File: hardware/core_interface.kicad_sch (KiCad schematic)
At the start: 2 parts, among them J90 Core_LGA, J91 Core_LGA

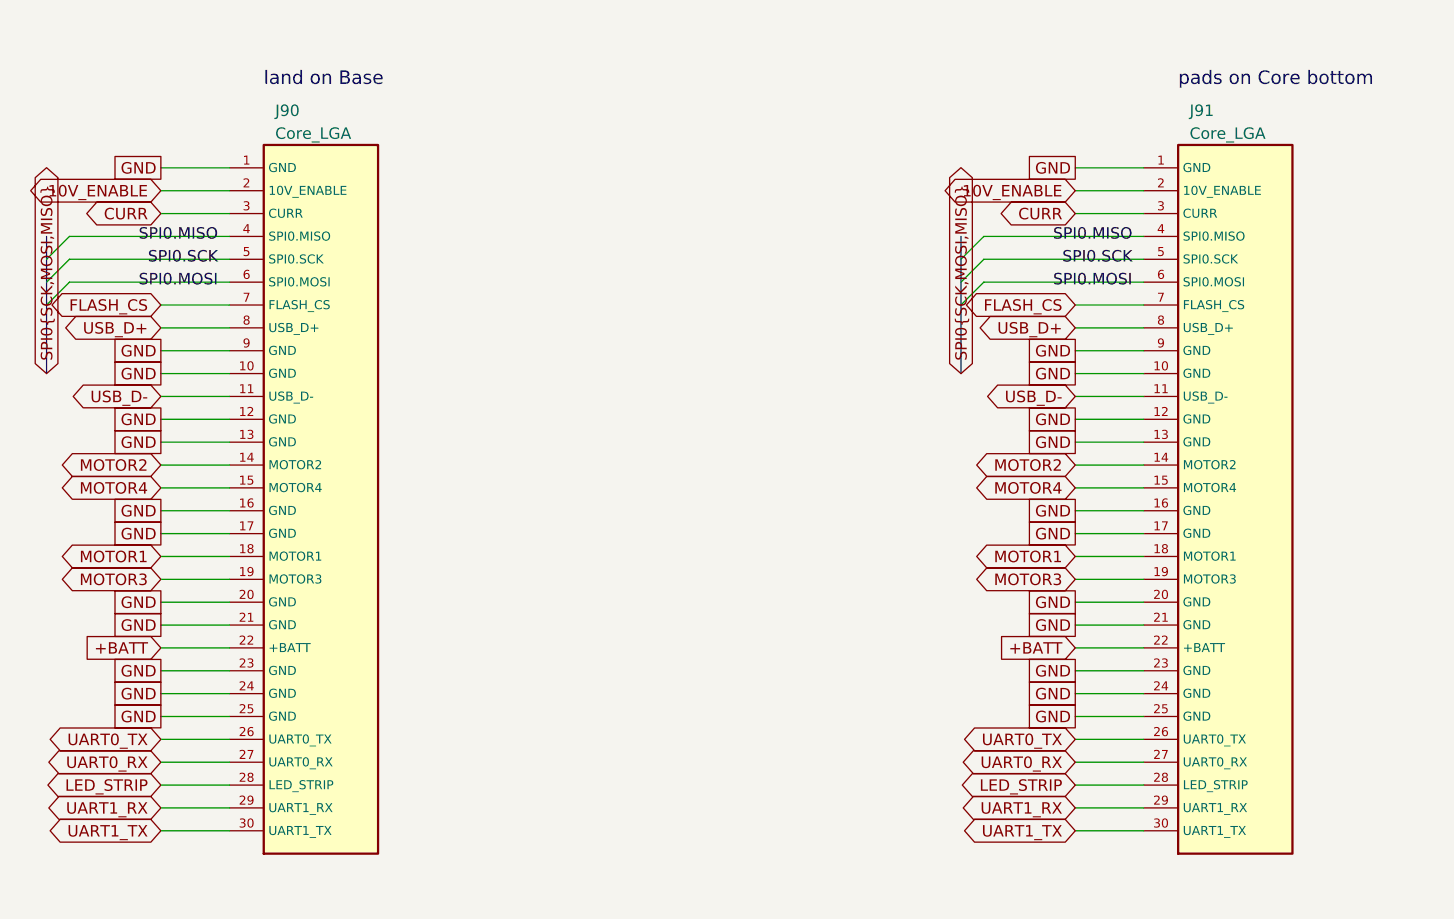
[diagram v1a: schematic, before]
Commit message: OpenAIO: LGA 31 pins (+5V and BUZZER- added, stray GND removed), J91 follows the pattern centre automatically
Co-Authored-By: Claude Fable 5 <noreply@anthropic.com>
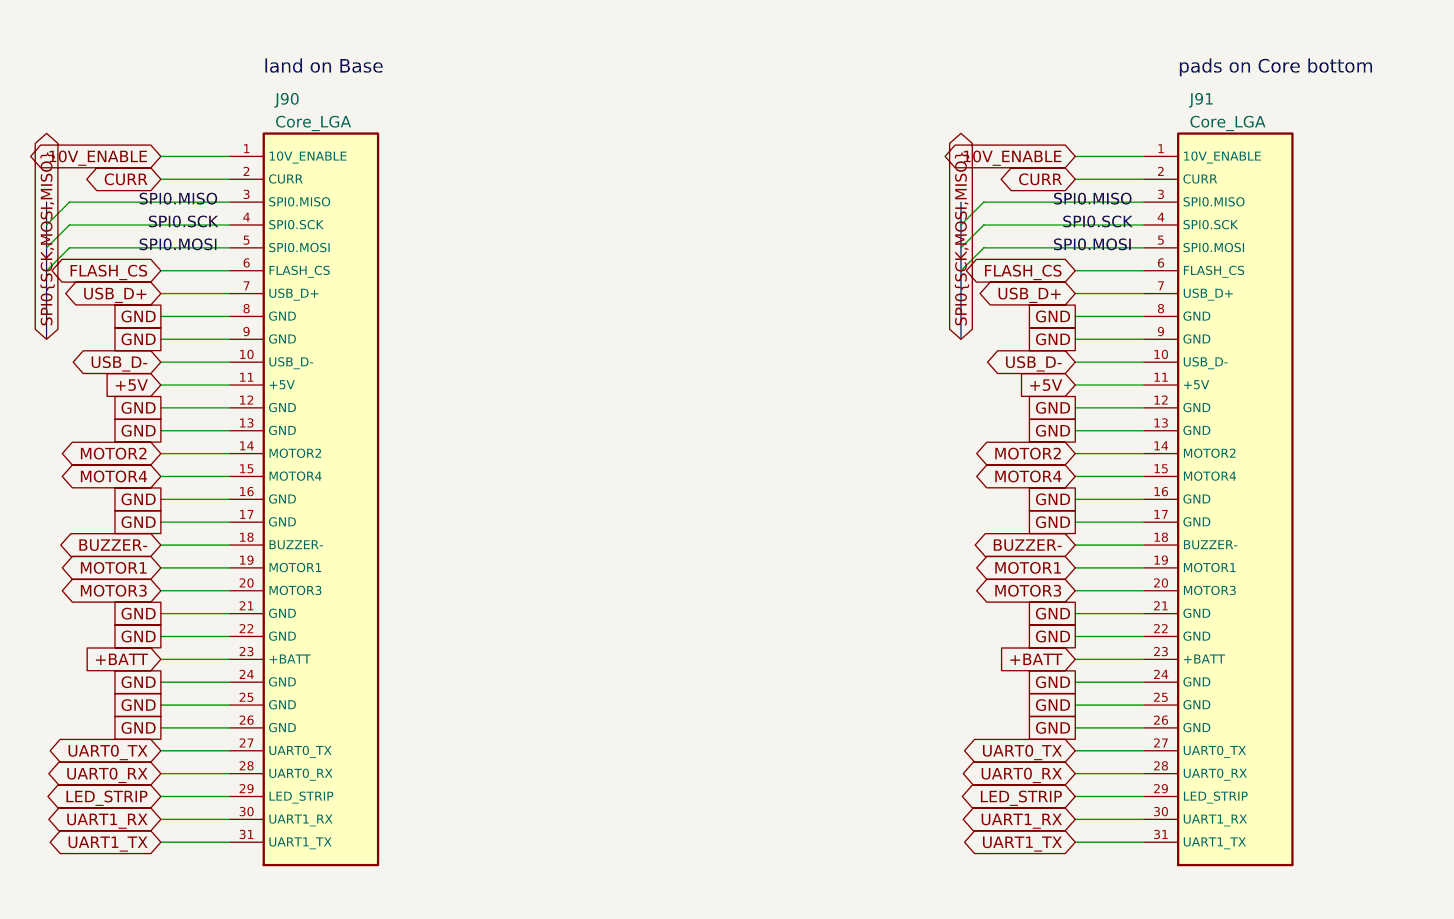
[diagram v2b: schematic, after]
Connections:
- net +BATT: now also J90.23 (+BATT), J91.23 (+BATT); no longer J90.22 (+BATT), J91.22 (+BATT)
- net 10V_ENABLE: now also J90.1 (10V_ENABLE), J91.1 (10V_ENABLE); no longer J90.2 (10V_ENABLE), J91.2 (10V_ENABLE)
- net CURR: now also J90.2 (CURR), J91.2 (CURR); no longer J90.3 (CURR), J91.3 (CURR)
- net FLASH_CS: now also J90.6 (FLASH_CS), J91.6 (FLASH_CS); no longer J90.7 (FLASH_CS), J91.7 (FLASH_CS)
- net GND: now also J90.22 (GND), J90.26 (GND), J90.8 (GND), J91.22 (GND), J91.26 (GND), J91.8 (GND); no longer J90.1 (GND), J90.10 (GND), J90.20 (GND), J90.23 (GND), J91.1 (GND), J91.10 (GND), J91.20 (GND), J91.23 (GND)
- net LED_STRIP: now also J90.29 (LED_STRIP), J91.29 (LED_STRIP); no longer J90.28 (LED_STRIP), J91.28 (LED_STRIP)
- net MOTOR1: now also J90.19 (MOTOR1), J91.19 (MOTOR1); no longer J90.18 (MOTOR1), J91.18 (MOTOR1)
- net MOTOR3: now also J90.20 (MOTOR3), J91.20 (MOTOR3); no longer J90.19 (MOTOR3), J91.19 (MOTOR3)
- net SPI0.MISO: now also J90.3 (SPI0.MISO), J91.3 (SPI0.MISO); no longer J90.4 (SPI0.MISO), J91.4 (SPI0.MISO)
- net SPI0.MOSI: now also J90.5 (SPI0.MOSI), J91.5 (SPI0.MOSI); no longer J90.6 (SPI0.MOSI), J91.6 (SPI0.MOSI)
- net SPI0.SCK: now also J90.4 (SPI0.SCK), J91.4 (SPI0.SCK); no longer J90.5 (SPI0.SCK), J91.5 (SPI0.SCK)
- net UART0_RX: now also J90.28 (UART0_RX), J91.28 (UART0_RX); no longer J90.27 (UART0_RX), J91.27 (UART0_RX)
- net UART0_TX: now also J90.27 (UART0_TX), J91.27 (UART0_TX); no longer J90.26 (UART0_TX), J91.26 (UART0_TX)
- net UART1_RX: now also J90.30 (UART1_RX), J91.30 (UART1_RX); no longer J90.29 (UART1_RX), J91.29 (UART1_RX)
- net UART1_TX: now also J90.31 (UART1_TX), J91.31 (UART1_TX); no longer J90.30 (UART1_TX), J91.30 (UART1_TX)
- net USB_D+: now also J90.7 (USB_D+), J91.7 (USB_D+); no longer J90.8 (USB_D+), J91.8 (USB_D+)
- net USB_D-: now also J90.10 (USB_D-), J91.10 (USB_D-); no longer J90.11 (USB_D-), J91.11 (USB_D-)
- new net +5V: J90.11 (+5V), J91.11 (+5V)
- new net BUZZER-: J90.18 (BUZZER-), J91.18 (BUZZER-)

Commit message: OpenAIO: LGA +10V pin added
Co-Authored-By: Claude Fable 5 <noreply@anthropic.com>
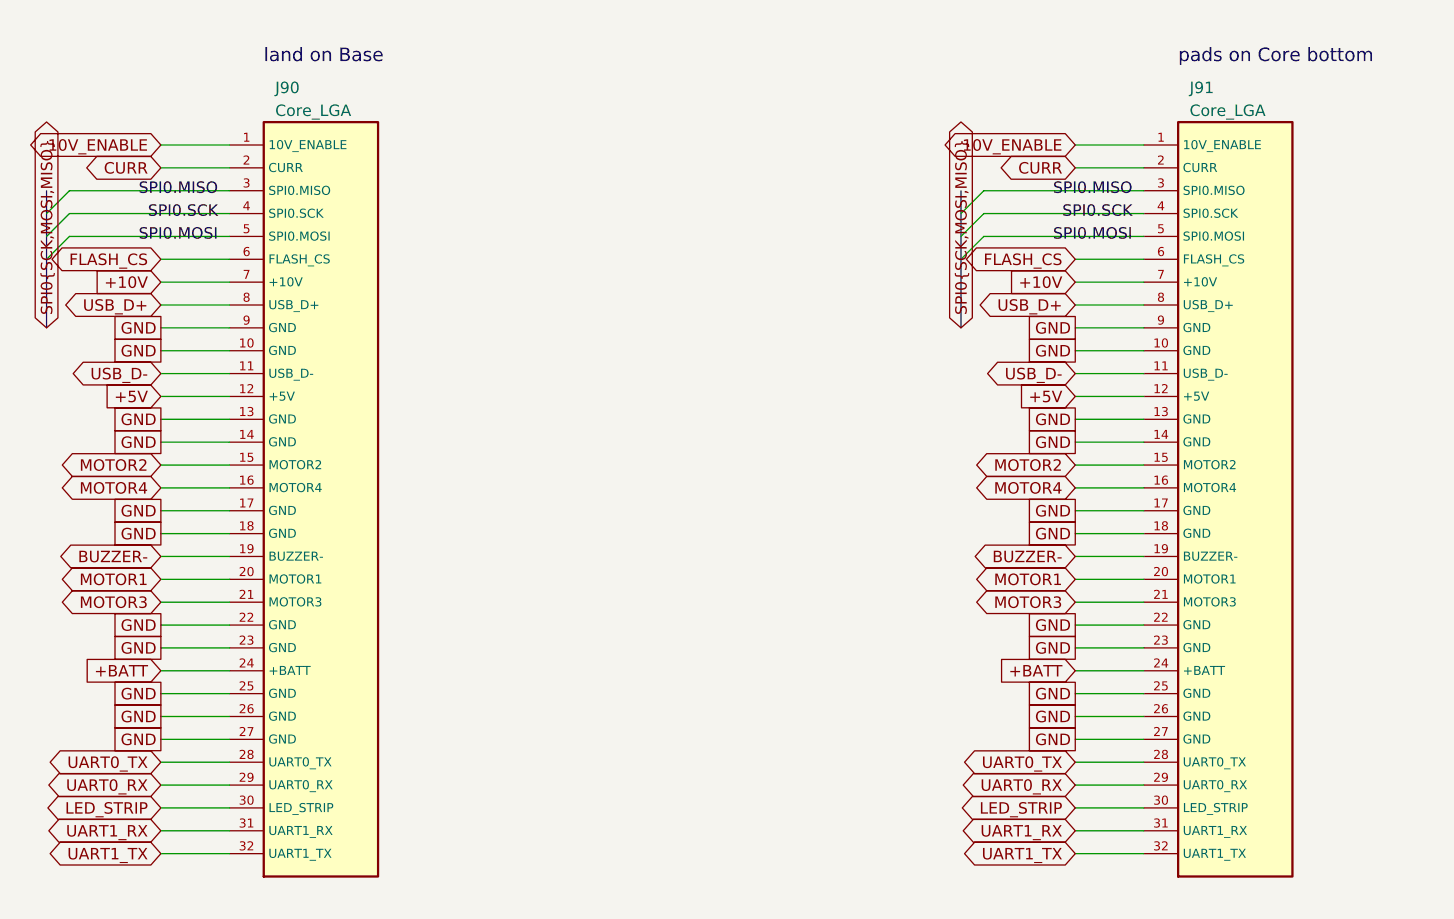
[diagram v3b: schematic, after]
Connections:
- net +5V: now also J90.12 (+5V), J91.12 (+5V); no longer J90.11 (+5V), J91.11 (+5V)
- net +BATT: now also J90.24 (+BATT), J91.24 (+BATT); no longer J90.23 (+BATT), J91.23 (+BATT)
- net BUZZER-: now also J90.19 (BUZZER-), J91.19 (BUZZER-); no longer J90.18 (BUZZER-), J91.18 (BUZZER-)
- net GND: now also J90.10 (GND), J90.14 (GND), J90.18 (GND), J90.23 (GND), J90.27 (GND), J91.10 (GND), J91.14 (GND), J91.18 (GND), J91.23 (GND), J91.27 (GND); no longer J90.12 (GND), J90.16 (GND), J90.21 (GND), J90.24 (GND), J90.8 (GND), J91.12 (GND), J91.16 (GND), J91.21 (GND), J91.24 (GND), J91.8 (GND)
- net LED_STRIP: now also J90.30 (LED_STRIP), J91.30 (LED_STRIP); no longer J90.29 (LED_STRIP), J91.29 (LED_STRIP)
- net MOTOR1: now also J90.20 (MOTOR1), J91.20 (MOTOR1); no longer J90.19 (MOTOR1), J91.19 (MOTOR1)
- net MOTOR2: now also J90.15 (MOTOR2), J91.15 (MOTOR2); no longer J90.14 (MOTOR2), J91.14 (MOTOR2)
- net MOTOR3: now also J90.21 (MOTOR3), J91.21 (MOTOR3); no longer J90.20 (MOTOR3), J91.20 (MOTOR3)
- net MOTOR4: now also J90.16 (MOTOR4), J91.16 (MOTOR4); no longer J90.15 (MOTOR4), J91.15 (MOTOR4)
- net UART0_RX: now also J90.29 (UART0_RX), J91.29 (UART0_RX); no longer J90.28 (UART0_RX), J91.28 (UART0_RX)
- net UART0_TX: now also J90.28 (UART0_TX), J91.28 (UART0_TX); no longer J90.27 (UART0_TX), J91.27 (UART0_TX)
- net UART1_RX: now also J90.31 (UART1_RX), J91.31 (UART1_RX); no longer J90.30 (UART1_RX), J91.30 (UART1_RX)
- net UART1_TX: now also J90.32 (UART1_TX), J91.32 (UART1_TX); no longer J90.31 (UART1_TX), J91.31 (UART1_TX)
- net USB_D+: now also J90.8 (USB_D+), J91.8 (USB_D+); no longer J90.7 (USB_D+), J91.7 (USB_D+)
- net USB_D-: now also J90.11 (USB_D-), J91.11 (USB_D-); no longer J90.10 (USB_D-), J91.10 (USB_D-)
- new net +10V: J90.7 (+10V), J91.7 (+10V)

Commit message: OpenAIO: LGA +3.3V pin added
Co-Authored-By: Claude Fable 5 <noreply@anthropic.com>
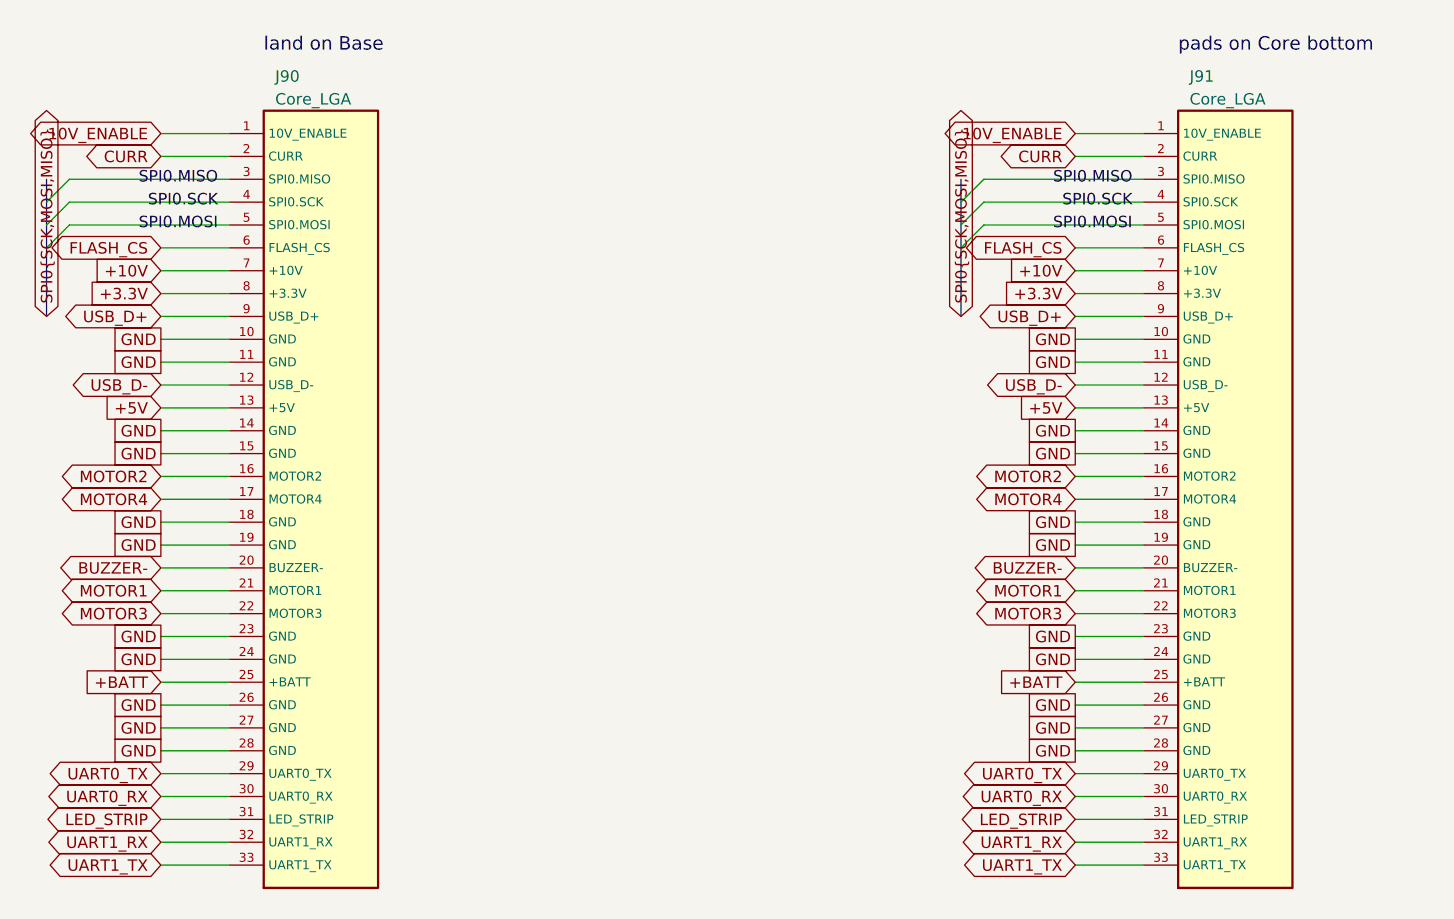
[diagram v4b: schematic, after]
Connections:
- net +5V: now also J90.13 (+5V), J91.13 (+5V); no longer J90.12 (+5V), J91.12 (+5V)
- net +BATT: now also J90.25 (+BATT), J91.25 (+BATT); no longer J90.24 (+BATT), J91.24 (+BATT)
- net BUZZER-: now also J90.20 (BUZZER-), J91.20 (BUZZER-); no longer J90.19 (BUZZER-), J91.19 (BUZZER-)
- net GND: now also J90.11 (GND), J90.15 (GND), J90.19 (GND), J90.24 (GND), J90.28 (GND), J91.11 (GND), J91.15 (GND), J91.19 (GND), J91.24 (GND), J91.28 (GND); no longer J90.13 (GND), J90.17 (GND), J90.22 (GND), J90.25 (GND), J90.9 (GND), J91.13 (GND), J91.17 (GND), J91.22 (GND), J91.25 (GND), J91.9 (GND)
- net LED_STRIP: now also J90.31 (LED_STRIP), J91.31 (LED_STRIP); no longer J90.30 (LED_STRIP), J91.30 (LED_STRIP)
- net MOTOR1: now also J90.21 (MOTOR1), J91.21 (MOTOR1); no longer J90.20 (MOTOR1), J91.20 (MOTOR1)
- net MOTOR2: now also J90.16 (MOTOR2), J91.16 (MOTOR2); no longer J90.15 (MOTOR2), J91.15 (MOTOR2)
- net MOTOR3: now also J90.22 (MOTOR3), J91.22 (MOTOR3); no longer J90.21 (MOTOR3), J91.21 (MOTOR3)
- net MOTOR4: now also J90.17 (MOTOR4), J91.17 (MOTOR4); no longer J90.16 (MOTOR4), J91.16 (MOTOR4)
- net UART0_RX: now also J90.30 (UART0_RX), J91.30 (UART0_RX); no longer J90.29 (UART0_RX), J91.29 (UART0_RX)
- net UART0_TX: now also J90.29 (UART0_TX), J91.29 (UART0_TX); no longer J90.28 (UART0_TX), J91.28 (UART0_TX)
- net UART1_RX: now also J90.32 (UART1_RX), J91.32 (UART1_RX); no longer J90.31 (UART1_RX), J91.31 (UART1_RX)
- net UART1_TX: now also J90.33 (UART1_TX), J91.33 (UART1_TX); no longer J90.32 (UART1_TX), J91.32 (UART1_TX)
- net USB_D+: now also J90.9 (USB_D+), J91.9 (USB_D+); no longer J90.8 (USB_D+), J91.8 (USB_D+)
- net USB_D-: now also J90.12 (USB_D-), J91.12 (USB_D-); no longer J90.11 (USB_D-), J91.11 (USB_D-)
- new net +3.3V: J90.8 (+3.3V), J91.8 (+3.3V)

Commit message: OpenAIO: LGA +4v5 pin added
Co-Authored-By: Claude Fable 5 <noreply@anthropic.com>
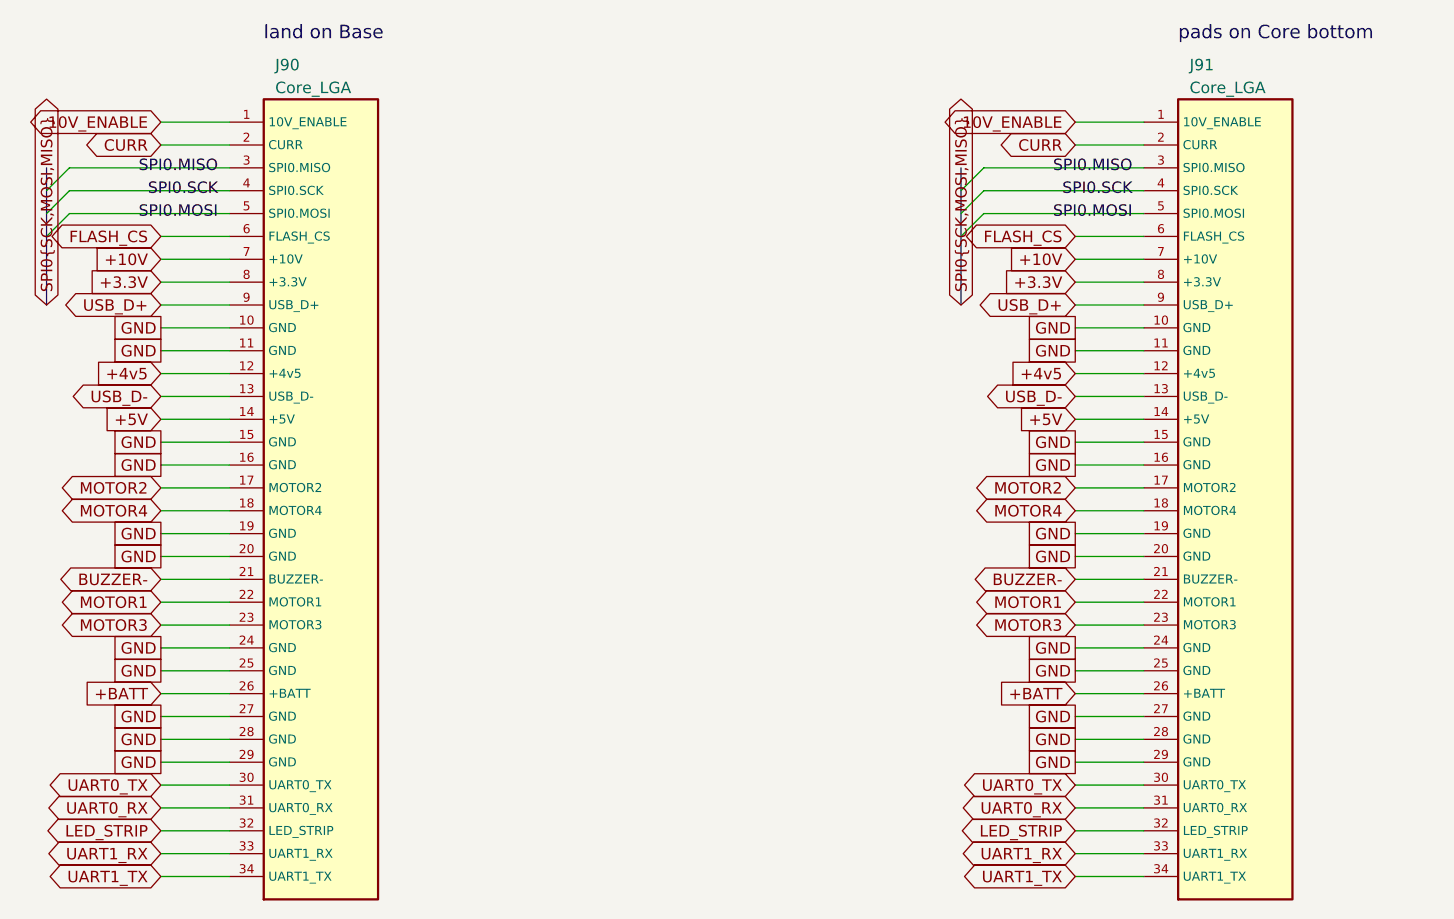
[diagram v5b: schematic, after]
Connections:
- net +5V: now also J90.14 (+5V), J91.14 (+5V); no longer J90.13 (+5V), J91.13 (+5V)
- net +BATT: now also J90.26 (+BATT), J91.26 (+BATT); no longer J90.25 (+BATT), J91.25 (+BATT)
- net BUZZER-: now also J90.21 (BUZZER-), J91.21 (BUZZER-); no longer J90.20 (BUZZER-), J91.20 (BUZZER-)
- net GND: now also J90.16 (GND), J90.20 (GND), J90.25 (GND), J90.29 (GND), J91.16 (GND), J91.20 (GND), J91.25 (GND), J91.29 (GND); no longer J90.14 (GND), J90.18 (GND), J90.23 (GND), J90.26 (GND), J91.14 (GND), J91.18 (GND), J91.23 (GND), J91.26 (GND)
- net LED_STRIP: now also J90.32 (LED_STRIP), J91.32 (LED_STRIP); no longer J90.31 (LED_STRIP), J91.31 (LED_STRIP)
- net MOTOR1: now also J90.22 (MOTOR1), J91.22 (MOTOR1); no longer J90.21 (MOTOR1), J91.21 (MOTOR1)
- net MOTOR2: now also J90.17 (MOTOR2), J91.17 (MOTOR2); no longer J90.16 (MOTOR2), J91.16 (MOTOR2)
- net MOTOR3: now also J90.23 (MOTOR3), J91.23 (MOTOR3); no longer J90.22 (MOTOR3), J91.22 (MOTOR3)
- net MOTOR4: now also J90.18 (MOTOR4), J91.18 (MOTOR4); no longer J90.17 (MOTOR4), J91.17 (MOTOR4)
- net UART0_RX: now also J90.31 (UART0_RX), J91.31 (UART0_RX); no longer J90.30 (UART0_RX), J91.30 (UART0_RX)
- net UART0_TX: now also J90.30 (UART0_TX), J91.30 (UART0_TX); no longer J90.29 (UART0_TX), J91.29 (UART0_TX)
- net UART1_RX: now also J90.33 (UART1_RX), J91.33 (UART1_RX); no longer J90.32 (UART1_RX), J91.32 (UART1_RX)
- net UART1_TX: now also J90.34 (UART1_TX), J91.34 (UART1_TX); no longer J90.33 (UART1_TX), J91.33 (UART1_TX)
- net USB_D-: now also J90.13 (USB_D-), J91.13 (USB_D-); no longer J90.12 (USB_D-), J91.12 (USB_D-)
- new net +4v5: J90.12 (+4v5), J91.12 (+4v5)
